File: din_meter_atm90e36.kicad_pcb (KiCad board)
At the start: 2 copper layers, 32 x 31.1 mm, 50 parts, among them IC1 ATM90E36_ATM90E36, IC2 ATM90E36_ATM90E36, J1 GS3, J2 GS3, J3 GS3, J4 GS3, J5 GS3, J6 GS3, Y1 Crystal_GND24, Y2 Crystal_GND24

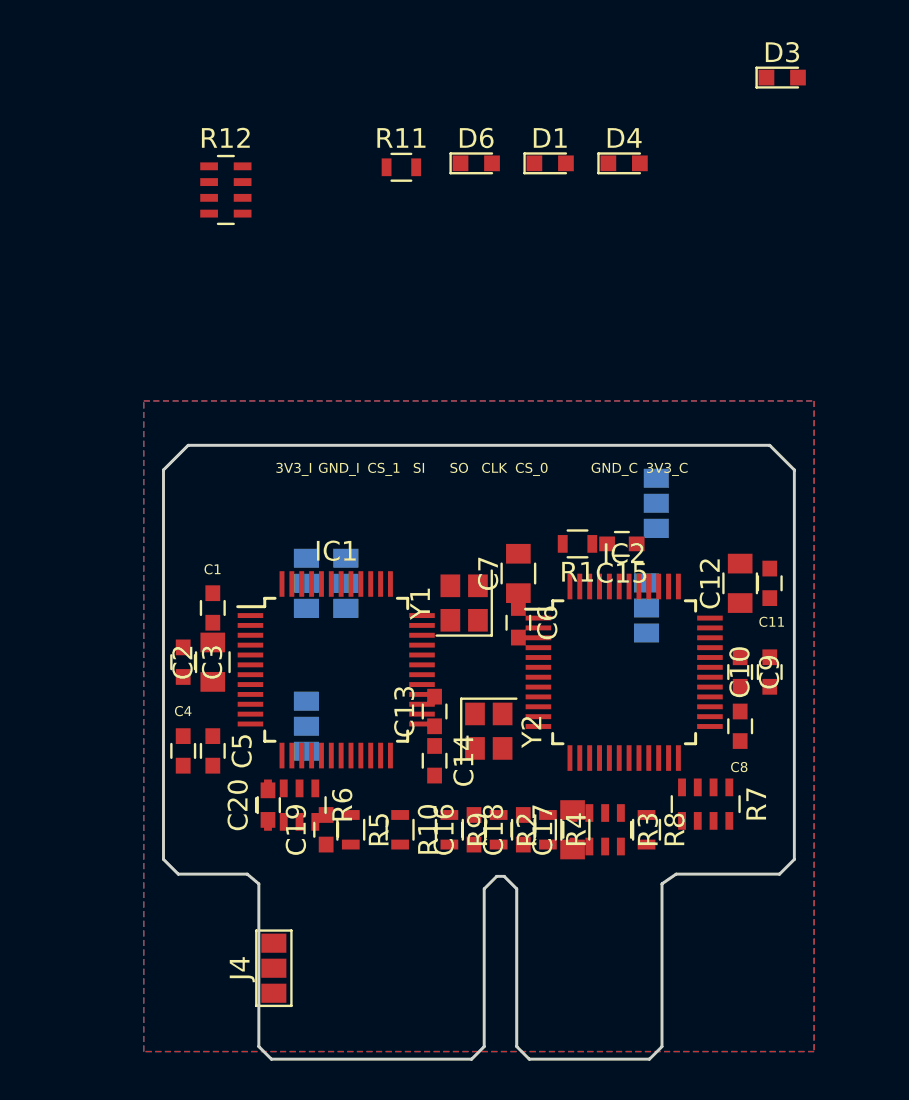
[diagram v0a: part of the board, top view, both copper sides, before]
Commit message: Make passives smaller
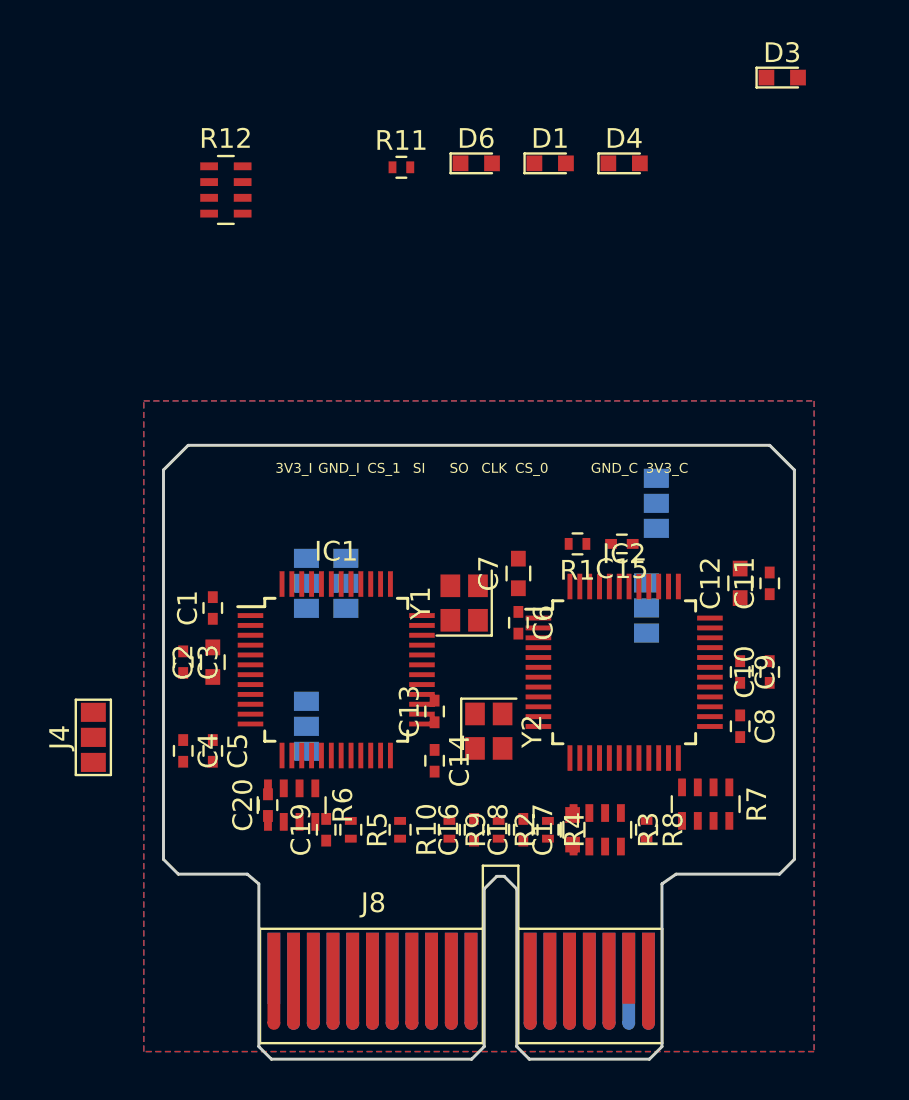
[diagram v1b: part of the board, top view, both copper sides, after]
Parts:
- added J8: Conn_02x18_Row_Letter_First, Connectors:PCI-EXPRESS, F.Cu at (135.5, 84.9)
- C1, C10, C11, C13, C14, C15, C16, C18, C19, C20, C3, C4, C5, C6, C8, C9: footprint Capacitors_SMD:C_0603 -> Capacitors_SMD:C_0402
- C12, C17, C2, C7: footprint Capacitors_SMD:C_0805 -> Capacitors_SMD:C_0603
- R1, R10, R11, R2, R4, R5, R8, R9: footprint Resistors_SMD:R_0603 -> Resistors_SMD:R_0402
- moved J4 14.9 mm to (126.4, 73.2)

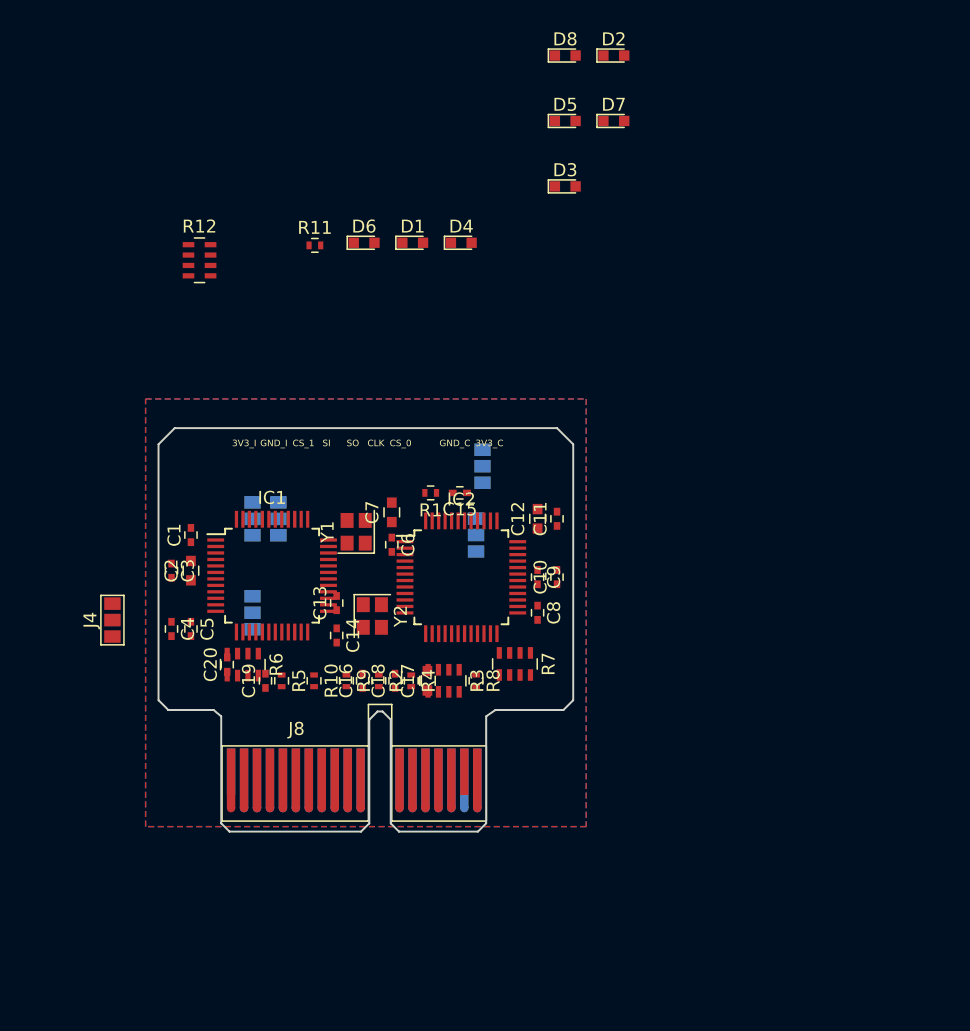
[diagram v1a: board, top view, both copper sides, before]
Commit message: Create sub-sheets and start layout
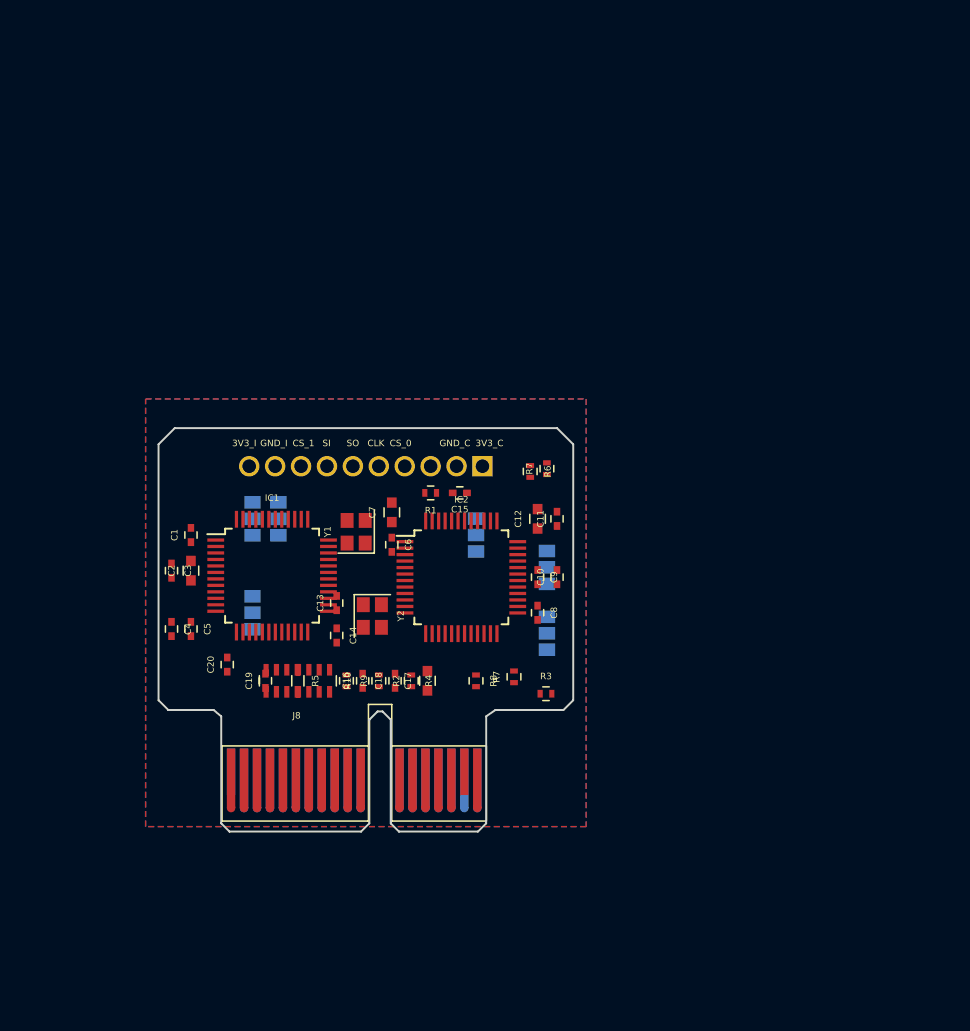
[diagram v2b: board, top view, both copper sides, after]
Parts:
- removed D1, D2, D3, D4, D5, D6, D7, D8: LED, LEDs:LED_0603
- removed R11: R, Resistors_SMD:R_0402
- removed R12: SMD-RES-ARRAY, Resistors_SMD:R_Array_Concave_4x0603
- removed the R7 at (157.4, 76.6)
- added J7: Conn_01x10, Molex_board2board:SHDR10W60P200_1X10_2150X400X335P, B.Cu at (154.9, 61.3)
- added R7: R, Resistors_SMD:R_0402, F.Cu at (159.9, 61.5)
- added R7: R, Resistors_SMD:R_0402, F.Cu at (157.3, 77.6)
- J4: moved to B.Cu
- R10, R5: value R -> SMD-RES-ARRAY; footprint Resistors_SMD:R_0402 -> Resistors_SMD:R_Array_Concave_4x0603
- R3, R6: value SMD-RES-ARRAY -> R; footprint Resistors_SMD:R_Array_Concave_4x0603 -> Resistors_SMD:R_0402
- moved J4 33.8 mm to (159.9, 69.2)
- moved R6 26.7 mm to (158.6, 61.7)
- moved J5 13.8 mm to (159.9, 74.2)
- moved R3 7.96 mm to (159.8, 78.9), turned to 0 degrees
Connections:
- IC1 pad 10: IN -> IN_0
- IC1 pad 22: ZX0 -> ZX0_0
- IC1 pad 23: ZX1 -> ZX1_0
- IC1 pad 24: ZX2 -> ZX2_0
- IC1 pad 25: CF1 -> CF1_0
- IC1 pad 26: CF2 -> CF2_0
- IC1 pad 27: CF3 -> CF3_0
- IC1 pad 28: CF4 -> CF4_0
- IC1 pad 29: WARN -> WARN_0
- IC1 pad 3: I1P -> I1P_0
- IC1 pad 30: IRQ2 -> IRQ2_0
- IC1 pad 31: IRQ1 -> IRQ1_0
- IC1 pad 33: PM0 -> PM0_0
- IC1 pad 34: PM1 -> PM1_0
- IC1 pad 36: DMA -> DMA_0
- IC1 pad 37: CS -> CS_0
- IC1 pad 4: I1N -> I1N_0
- IC1 pad 5: I2P -> I2P_0
- IC1 pad 6: I2N -> I2N_0
- IC1 pad 7: I3P -> I3P_0
- IC1 pad 8: I3N -> I3N_0
- IC1 pad 9: IP -> IP_0
- IC2 pad 22: ZX0 -> ZX0_1
- IC2 pad 23: ZX1 -> ZX1_1
- IC2 pad 24: ZX2 -> ZX2_1
- IC2 pad 25: CF1 -> CF1_1
- IC2 pad 26: CF2 -> CF2_1
- IC2 pad 27: CF3 -> CF3_1
- IC2 pad 28: CF4 -> CF4_1
- IC2 pad 29: WARN -> WARN_1
- IC2 pad 30: IRQ2 -> IRQ2_1
- IC2 pad 31: IRQ1 -> IRQ1_1
- IC2 pad 33: PM0 -> PM0_1
- IC2 pad 34: PM1 -> PM1_1
- IC2 pad 36: DMA -> DMA_1
- IC2 pad 37: CS -> CS_1
- J1 pad 2: DMA -> DMA_0
- J2 pad 2: PM0 -> PM0_0
- J3 pad 2: PM1 -> PM1_0
- J4 pad 2: DMA -> DMA_1
- J5 pad 2: PM0 -> PM0_1
- J6 pad 2: PM1 -> PM1_1
- R10 pad 2: Net-(C18-Pad1) -> +3V3
- R3 pad 1: CF4 -> +3V3
- R3 pad 2: CF3 -> Net-(C8-Pad1)
- R4 pad 1: +3V3 -> Net-(C10-Pad2)
- R4 pad 2: Net-(C8-Pad1) -> GND
- R5 pad 1: Net-(C10-Pad2) -> +3V3
- R5 pad 2: GND -> +3V3
- R6 pad 1: +3V3 -> Net-(C14-Pad2)
- R6 pad 2: +3V3 -> GND
- R8 pad 1: Net-(C14-Pad2) -> +3V3
- R8 pad 2: GND -> Net-(C18-Pad1)
- R9 pad 1: Net-(C19-Pad2) -> Net-(C20-Pad2)

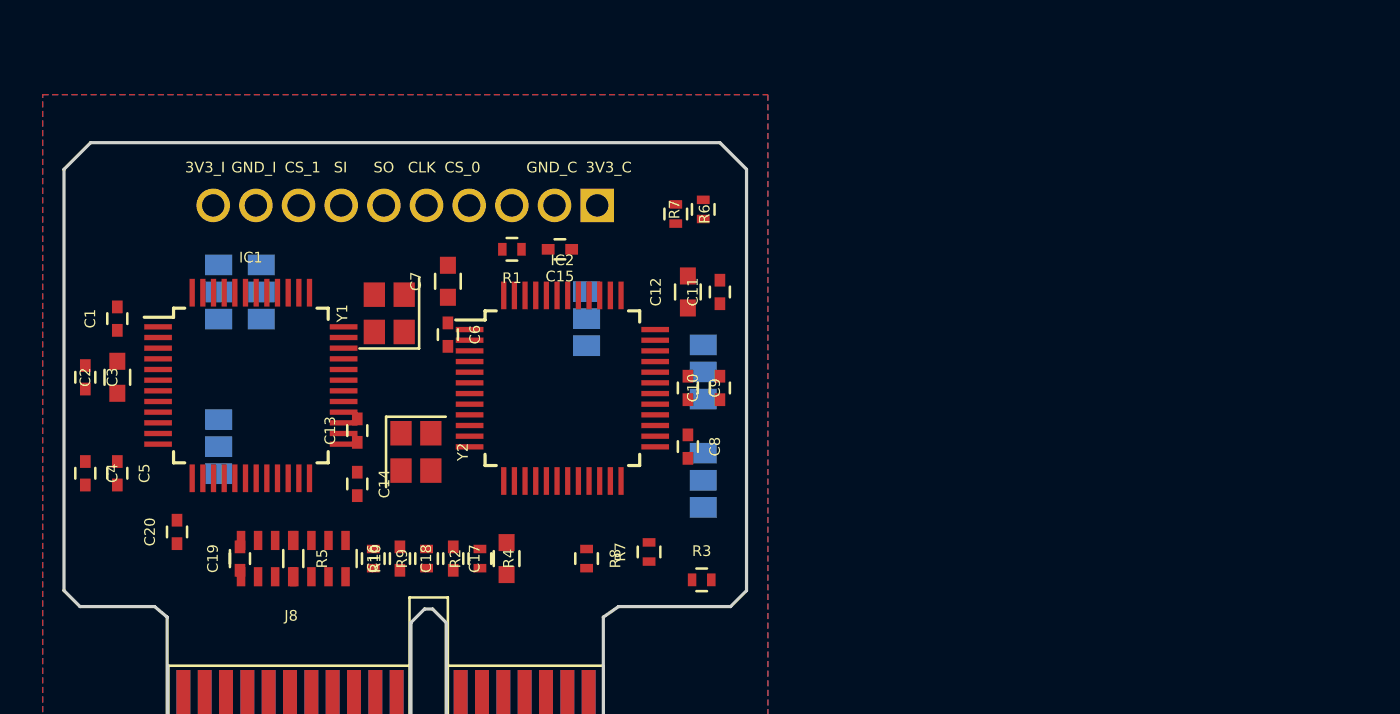
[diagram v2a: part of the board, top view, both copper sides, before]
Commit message: Wired up current samplers
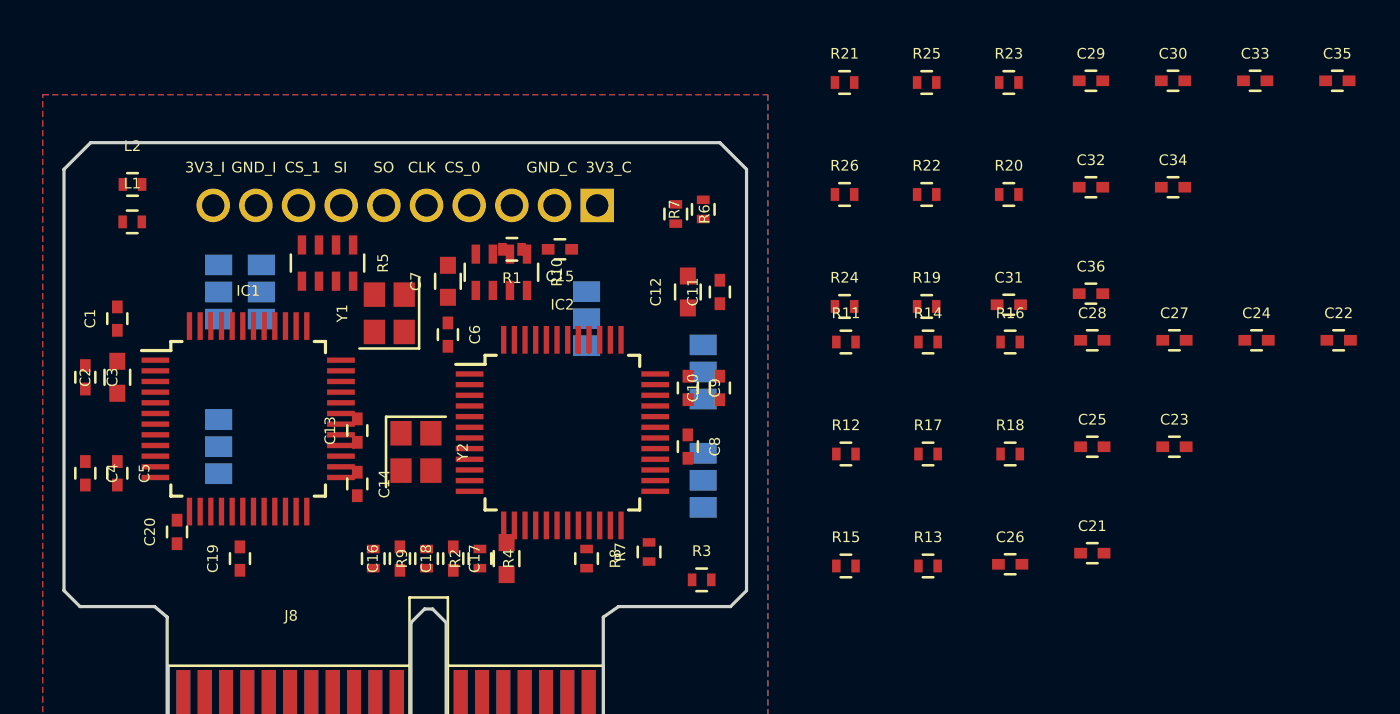
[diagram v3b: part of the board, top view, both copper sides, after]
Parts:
- added C21: 18n, Capacitors_SMD:C_0402, F.Cu at (178.1, 77.6)
- added C22: 18n, Capacitors_SMD:C_0402, F.Cu at (189.7, 67.7)
- added C23: 18n, Capacitors_SMD:C_0402, F.Cu at (182.0, 72.7)
- added C24: 18n, Capacitors_SMD:C_0402, F.Cu at (185.8, 67.7)
- added C25: 18n, Capacitors_SMD:C_0402, F.Cu at (178.1, 72.7)
- added C26: 18n, Capacitors_SMD:C_0402, F.Cu at (174.3, 78.2)
- added C27: 18n, Capacitors_SMD:C_0402, F.Cu at (182.0, 67.7)
- added C28: 18n, Capacitors_SMD:C_0402, F.Cu at (178.1, 67.7)
- added C29: 18n, Capacitors_SMD:C_0402, F.Cu at (178.1, 55.5)
- added C30: 18n, Capacitors_SMD:C_0402, F.Cu at (181.9, 55.5)
- added C31: 18n, Capacitors_SMD:C_0402, F.Cu at (174.2, 66.0)
- added C32: 18n, Capacitors_SMD:C_0402, F.Cu at (178.1, 60.5)
- added C33: 18n, Capacitors_SMD:C_0402, F.Cu at (185.8, 55.5)
- added C34: 18n, Capacitors_SMD:C_0402, F.Cu at (181.9, 60.5)
- added C35: 18n, Capacitors_SMD:C_0402, F.Cu at (189.6, 55.5)
- added C36: 18n, Capacitors_SMD:C_0402, F.Cu at (178.1, 65.5)
- added L1: L_Small, Inductors_SMD:L_0402, F.Cu at (133.1, 62.1)
- added L2: L_Small, Inductors_SMD:L_0402, F.Cu at (133.1, 60.4)
- added R11: 1K, Resistors_SMD:R_0402, F.Cu at (166.6, 67.7)
- added R12: 1K, Resistors_SMD:R_0402, F.Cu at (166.6, 73.0)
- added R13: 1K, Resistors_SMD:R_0402, F.Cu at (170.4, 78.2)
- added R14: 1K, Resistors_SMD:R_0402, F.Cu at (170.4, 67.7)
- added R15: 1K, Resistors_SMD:R_0402, F.Cu at (166.6, 78.2)
- added R16: 1K, Resistors_SMD:R_0402, F.Cu at (174.3, 67.7)
- added R17: 1K, Resistors_SMD:R_0402, F.Cu at (170.4, 73.0)
- added R18: 1K, Resistors_SMD:R_0402, F.Cu at (174.3, 73.0)
- added R19: 1K, Resistors_SMD:R_0402, F.Cu at (170.4, 66.1)
- added R20: 1K, Resistors_SMD:R_0402, F.Cu at (174.2, 60.8)
- added R21: 1K, Resistors_SMD:R_0402, F.Cu at (166.5, 55.6)
- added R22: 1K, Resistors_SMD:R_0402, F.Cu at (170.4, 60.8)
- added R23: 1K, Resistors_SMD:R_0402, F.Cu at (174.2, 55.6)
- added R24: 1K, Resistors_SMD:R_0402, F.Cu at (166.5, 66.1)
- added R25: 1K, Resistors_SMD:R_0402, F.Cu at (170.4, 55.6)
- added R26: 1K, Resistors_SMD:R_0402, F.Cu at (166.5, 60.8)
- moved R10 15.9 mm to (150.4, 64.5)
- moved R5 14.1 mm to (142.3, 64.0)
- moved IC2 2.08 mm to (153.3, 72.0)
- moved IC1 1.57 mm to (138.5, 71.3)
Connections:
- net Net-(J7-Pad1) renamed 3V3_CPU
- net Net-(J7-Pad2) renamed GND_CPU
- net Net-(J7-Pad3) renamed CS_2
- C16 pad 2: GND -> Net-(C16-Pad2)
- C17 pad 2: GND -> Net-(C17-Pad2)
- C6 pad 2: GND -> Net-(C6-Pad2)
- C7 pad 2: GND -> Net-(C7-Pad2)
- IC2 pad 10: IN -> IN_1
- IC2 pad 3: I1P -> I1P_1
- IC2 pad 4: I1N -> I1N_1
- IC2 pad 5: I2P -> I2P_1
- IC2 pad 6: I2N -> I2N_1
- IC2 pad 7: I3P -> I3P_1
- IC2 pad 8: I3N -> I3N_1
- IC2 pad 9: IP -> IP_1
- J7 pad 10: Net-(J7-Pad10) -> 3V3_ISO
- J7 pad 4: Net-(J7-Pad4) -> CS_0
- J7 pad 5: Net-(J7-Pad5) -> SCLK
- J7 pad 6: Net-(J7-Pad6) -> MISO
- J7 pad 7: Net-(J7-Pad7) -> MOSI
- J7 pad 8: Net-(J7-Pad8) -> CS_1
- J7 pad 9: Net-(J7-Pad9) -> GND_ISO
- R10 pad 2: +3V3 -> Net-(R10-Pad2)
- R10 pad 3: +3V3 -> Net-(R10-Pad3)
- R10 pad 4: +3V3 -> Net-(R10-Pad4)
- R5 pad 2: +3V3 -> Net-(R5-Pad2)
- R5 pad 3: +3V3 -> Net-(R5-Pad3)
- R5 pad 4: +3V3 -> Net-(R5-Pad4)
